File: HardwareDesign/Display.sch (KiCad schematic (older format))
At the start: 26 parts, among them J601 Conn_01x12, U601 Upduino_3.0

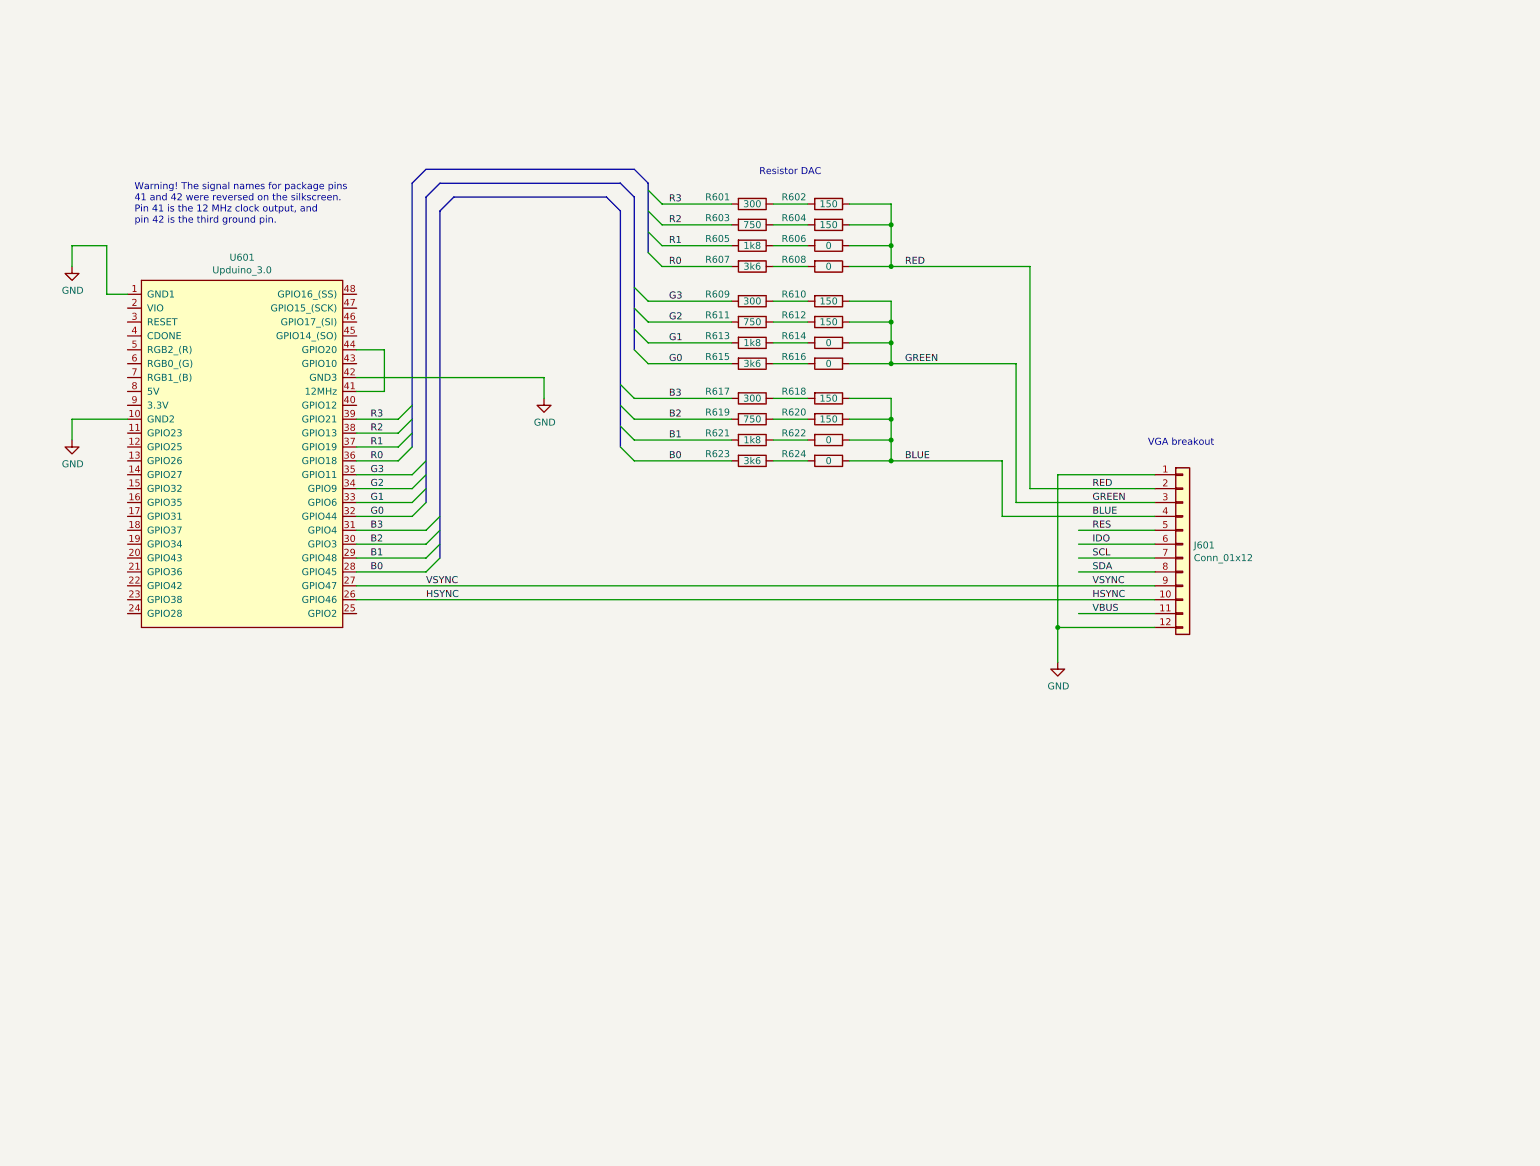
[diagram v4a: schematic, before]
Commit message: start interface from system to display FPGA
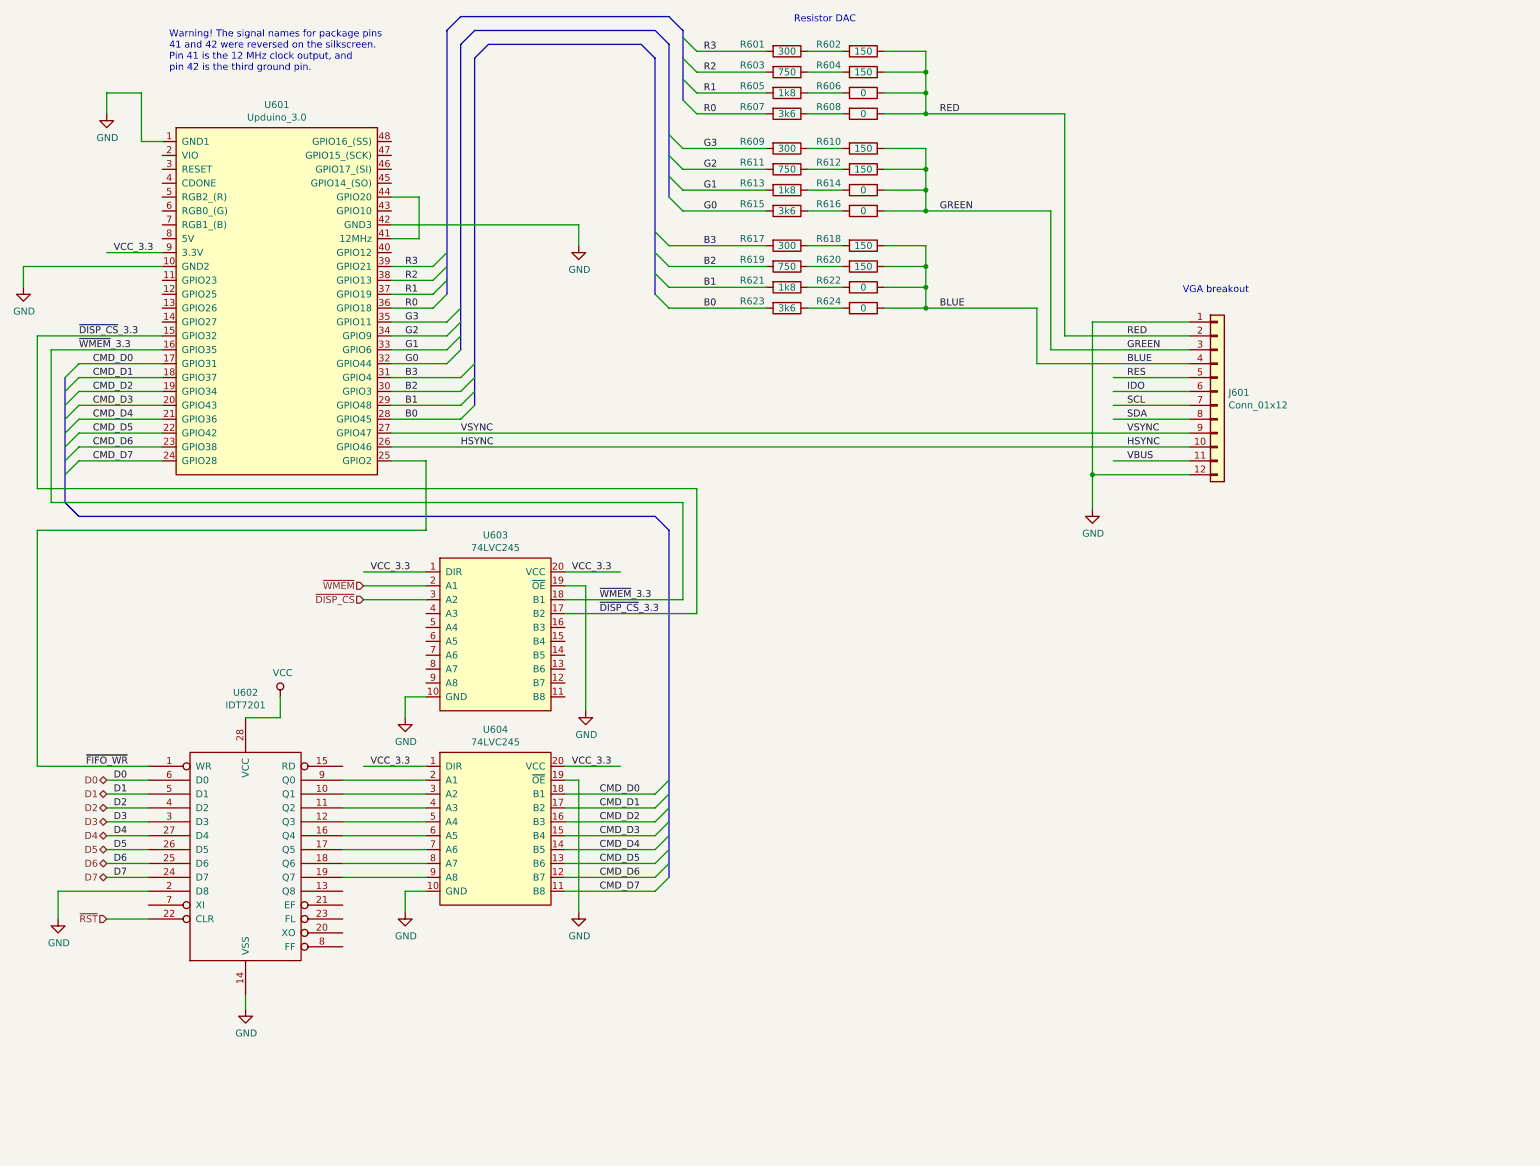
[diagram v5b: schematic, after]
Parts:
- added U602: IDT7201, symbol memory:IDT7201
- added U603, U604: 74LVC245, symbol 74LVC245:74LVC245
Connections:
- net labels added: CMD_D0, CMD_D1, CMD_D2, CMD_D3, CMD_D4, CMD_D5, CMD_D6, CMD_D7, D0, D1, D2, D3, D4, D5, D6, D7, VCC, VCC_3.3, ~DISP_CS~, ~DISP_CS~_3.3, ~FIFO_WR~, ~RST~, ~WMEM~, ~WMEM~_3.3
- wire segments 88 -> 156
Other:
- moved on the sheet: J601, R601, R602, R603, R604, R605, R606, R607, R608, R609, R610, R611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

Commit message: made display circuit a test using an Arduino Nano
Once communication between the Arduino and the FPGA
via the FIFO is working, then it will make sense to work
on interfacing with the actual host system.
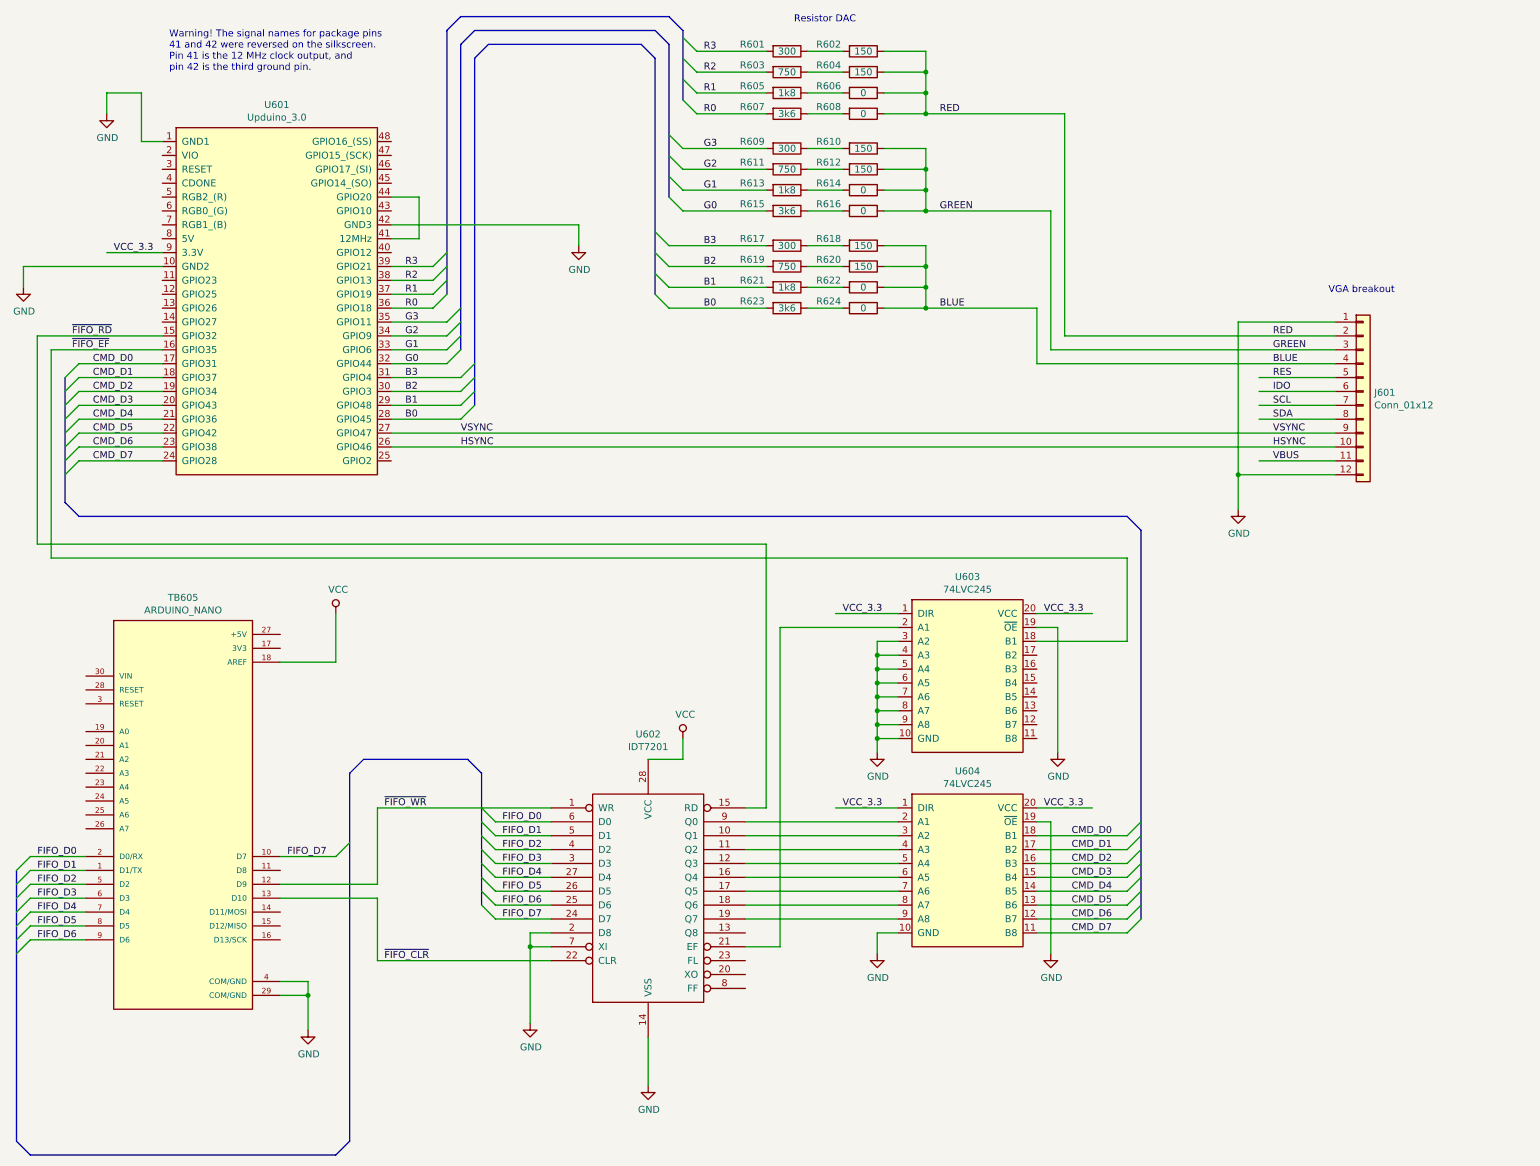
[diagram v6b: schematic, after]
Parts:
- added TB605: ARDUINO_NANO, SHIELD_ARDUINO_NANO, symbol ARDUINO_NANO:ARDUINO_NANO
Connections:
- net labels added: FIFO_D0, FIFO_D1, FIFO_D2, FIFO_D3, FIFO_D4, FIFO_D5, FIFO_D6, FIFO_D7, ~FIFO_CLR~, ~FIFO_EF~, ~FIFO_RD~
- net labels removed: D0, D1, D2, D3, D4, D5, D6, D7, ~DISP_CS~, ~DISP_CS~_3.3, ~RST~, ~WMEM~, ~WMEM~_3.3
- wire segments 156 -> 187
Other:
- moved on the sheet: J601, U602, U603, U604

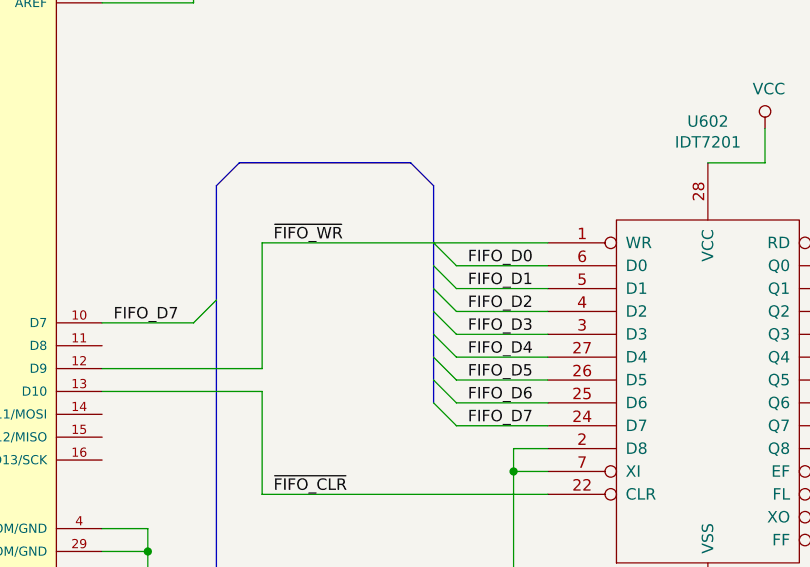
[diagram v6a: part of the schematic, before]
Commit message: fixed a minor ambiguity
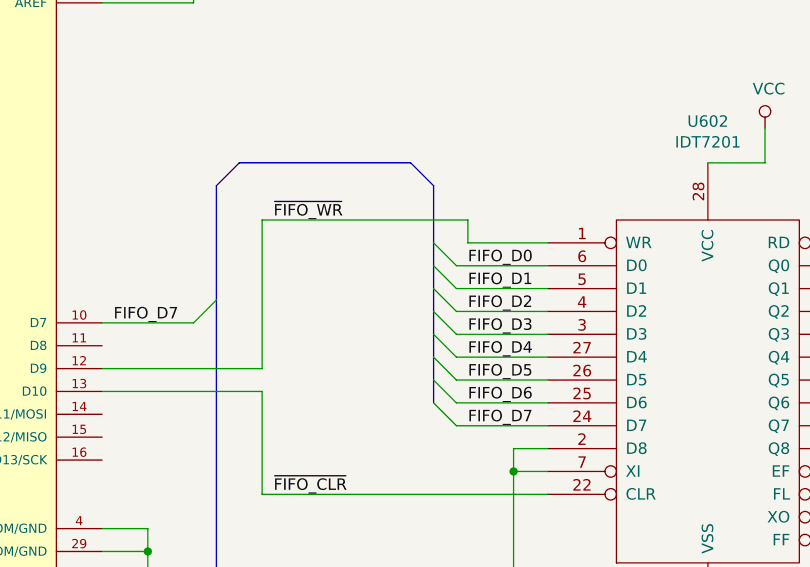
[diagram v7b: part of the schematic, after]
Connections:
- wire segments 187 -> 189
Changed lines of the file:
@@
 	4000 5950 3250 5950
-Wire Wire Line
-	3350 6300 3350 6850
 Wire Wire Line
 	3350 6850 2650 6850
@@
 Wire Wire Line
 	3350 6950 2650 6950
-Text Label 3400 6300 0    50   ~ 0
+Text Label 3400 6200 0    50   ~ 0
 ~FIFO_WR~
 Text Label 3400 7400 0    50   ~ 0
@@
 	6950 5700 6950 5800
 Wire Wire Line
-	3350 6300 4600 6300
+	3350 6200 4250 6200
+Wire Wire Line
+	4250 6200 4250 6300
+Wire Wire Line
+	4250 6300 4600 6300
+Wire Wire Line
+	3350 6200 3350 6850
 Wire Bus Line
 	3150 6050 3150 8700

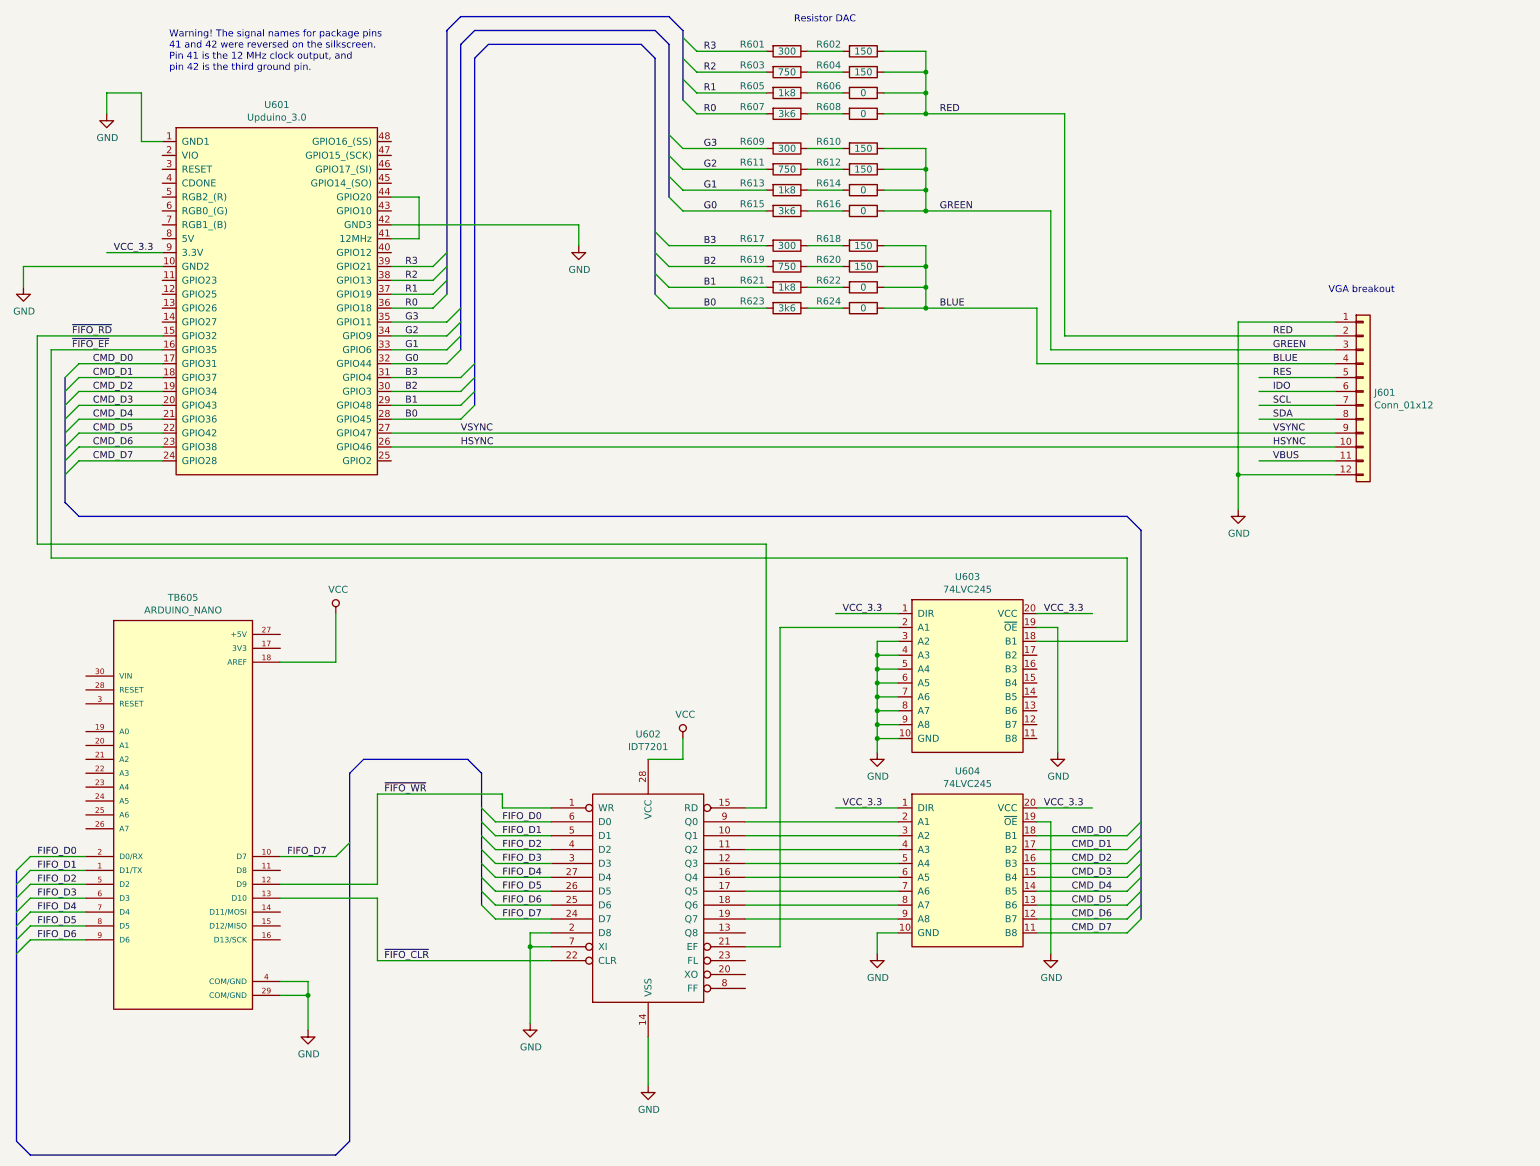
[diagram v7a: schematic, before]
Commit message: minor changes to display test circuit
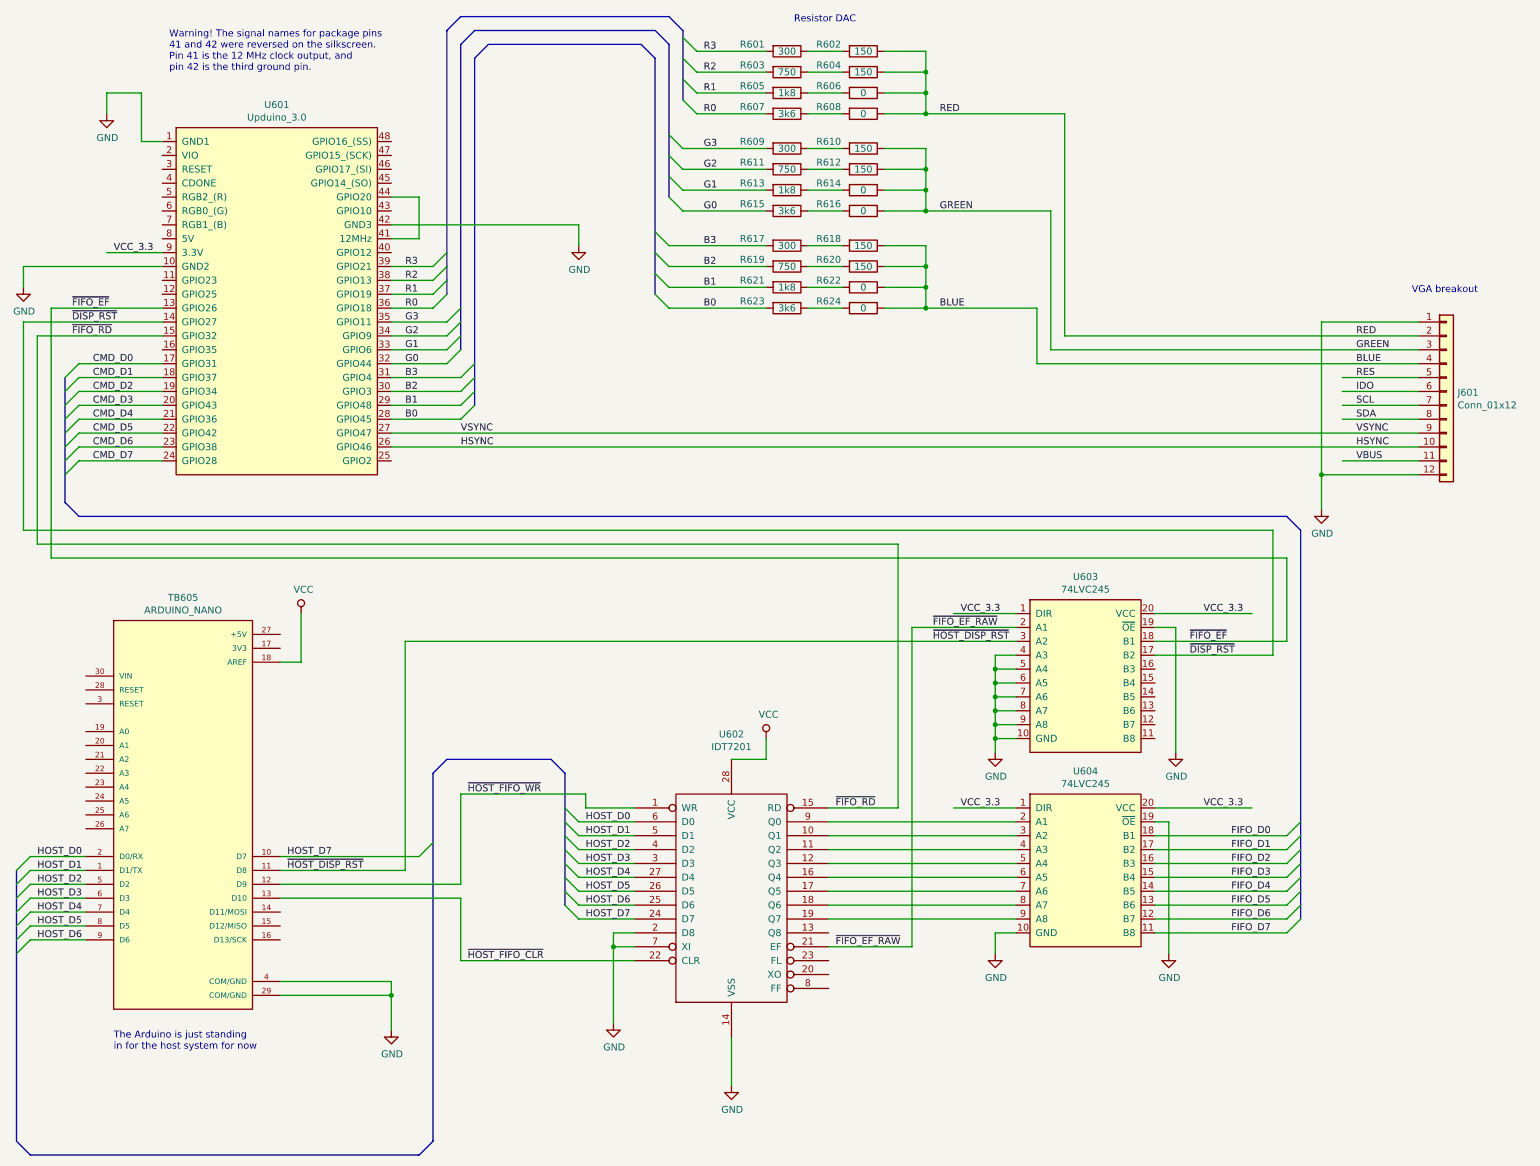
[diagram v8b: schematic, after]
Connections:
- net labels added: HOST_D0, HOST_D1, HOST_D2, HOST_D3, HOST_D4, HOST_D5, HOST_D6, HOST_D7, ~DISP_RST~, ~FIFO_EF_RAW~, ~HOST_DISP_RST~, ~HOST_FIFO_CLR~, ~HOST_FIFO_WR~
- net labels removed: ~FIFO_CLR~, ~FIFO_WR~
- wire segments 189 -> 195
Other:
- note added: "The Arduino is just standing\nin for the host system for now"
- moved on the sheet: J601, U602, U603, U604
